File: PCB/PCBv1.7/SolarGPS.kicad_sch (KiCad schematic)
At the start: 38 parts, among them J1 Conn_01x10_Female, J2 GND, J3 GND, J4 Solar1+, J5 Solar2+, J6 Conn_02x03_Odd_Even, J7 Screw_Terminal_01x01, J8 Conn_01x04_Male, SW1 SW_Push, U1 TPS63802, U2 SAM-M10Q, U3 STM32L071KBTx, U4 MAX40200AUK, Y1 32.768

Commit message: Submit board 1.7
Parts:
- removed D1, D2: Schottky, Diode_SMD:D_SOD-323_HandSoldering, symbol Device:D_Schottky_Small
- removed U4: MAX40200AUK, Package_TO_SOT_SMD:SOT-23-5, symbol Analog_Switch:MAX40200AUK
- added D1: 4V, Diode_SMD:D_SMB_Handsoldering, symbol Device:D_Zener
- added U4, U5, U6: LM66100, Package_TO_SOT_SMD:SOT-363_SC-70-6, symbol Heliograph:LM66100
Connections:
- net GND: now also D1.2 (A), U4.2 (GND), U4.5 (ST), U5.2 (GND), U5.5 (ST), U6.2 (GND), U6.5 (ST)
- net GPS_EN: now also U4.3 (EN)
- net GPS_VDD: now also U4.6 (OUT)
- net SOLAR1+: now also U5.1 (VDD)
- net SOLAR2+: now also U6.1 (VDD)
- net VBAT: now also D1.1 (K), U5.3 (EN), U5.6 (OUT), U6.3 (EN), U6.6 (OUT)
- net VDD: now also U4.1 (VDD)
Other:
- moved on the sheet: C1, C10, C4, C5, C6, C7, C8, C9, J3, J5, L1, R2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

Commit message: Tweak PCB
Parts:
- removed D1: 4V, Diode_SMD:D_SMB_Handsoldering, symbol Device:D_Zener
- removed R4: 432k, Resistor_SMD:R_0603_1608Metric, symbol Device:R_Small
- removed SW1: SW_Push, Button_Switch_SMD:SW_SPST_CK_RS282G05A3, symbol Switch:SW_Push
- removed U4, U5, U6: LM66100, Package_TO_SOT_SMD:SOT-363_SC-70-6, symbol Heliograph:LM66100
- added C11: 1uF, Capacitor_SMD:C_0603_1608Metric, symbol Device:C_Small
- added D3: LED_Small, Diode_SMD:D_0805_2012Metric, symbol Device:LED_Small
- added R5: 60, Resistor_SMD:R_0603_1608Metric, symbol Device:R_Small
- added U4: BMI160, digikey-footprints:BMI160, symbol dk_Motion-Sensors-IMUs-Inertial-Measurement-Units:BMI160
- added U5, U6, U7: MAX40200AUK, Package_TO_SOT_SMD:SOT-23-5, symbol Analog_Switch:MAX40200AUK
- C7: value 0.1uF -> 1uF
- R1: value 100 -> 86k
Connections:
- net DISPCS: now also U3.20 (PA10); no longer U3.19 (PA9)
- net GND: now also C11.2, U4.6 (GND), U4.7 (GND), U5.2 (GND), U6.2 (GND), U7.2 (GND)
- net GPS_EN: now also U5.3 (EN)
- net GPS_VDD: now also U5.5 (OUT)
- net LCDEN: now also U3.19 (PA9); no longer U3.18 (PA8)
- net SOLAR1+: now also U6.1 (VDD)
- net SOLAR2+: now also U7.1 (VDD)
- net SPI_CLK: now also U4.13 (SC)
- net SPI_MISO: now also U4.1 (SDO)
- net SPI_MOSI: now also U4.14 (SD)
- net VBAT: now also U6.5 (OUT), U7.5 (OUT)
- net VDD: now also C11.1, R5.1, U4.5 (VDDIO), U4.8 (VDD), U5.1 (VDD)
- net MMU_INT: now reaches U3.14 (PB0)
- net MMU_INT: now also U4.4 (INT1)
- net MMU_CS: now reaches U3.15 (PB1)
- net MMU_CS: now also U4.12 (CSB)
- net LED: now reaches U3.22 (PA12)
- net LED: now also D3.1 (K)
- net Button: no longer names the net of U3.6 (PA0)
- new net: D3.2 (A), R5.2
- new net SOLAREN: U3.18 (PA8), U6.3 (EN), U7.3 (EN)
- no-connect marks 9 -> 20
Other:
- note added: "VEN = 1.1V"
- moved on the sheet: C1, C5, J2, J3, J4, J5, U2

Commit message: add USB!
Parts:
- removed C11, C19: 1uF, Capacitor_SMD:C_0603_1608Metric, symbol Device:C_Small
- removed C5: 4.7uF, Capacitor_SMD:C_0805_2012Metric, symbol Device:C_Small
- removed U3: STM32L071KBTx, Package_QFP:LQFP-32_7x7mm_P0.8mm, symbol MCU_ST_STM32L0:STM32L071KBTx
- added C12, C17: 1uF, Capacitor_SMD:C_0603_1608Metric, symbol Device:C_Small
- added D1: LED_Small, Diode_SMD:D_0805_2012Metric, symbol Device:LED_Small
- added J9: USB_C_Receptacle_USB2.0, Veridian:USB_TYPE_C_PCB, symbol Connector:USB_C_Receptacle_USB2.0
- added R10: 10, Resistor_SMD:R_0805_2012Metric, symbol Device:R_Small
- added R11, R8, R9: 5.1K, Resistor_SMD:R_0603_1608Metric, symbol Device:R_Small
- added R4, R?: 86k, Resistor_SMD:R_0603_1608Metric, symbol Device:R_Small
- added U3: STM32L432KCUx, Package_DFN_QFN:QFN-32-1EP_5x5mm_P0.5mm_EP3.45x3.45mm, symbol MCU_ST_STM32L4:STM32L432KCUx
- added U8: USBLC6-2SC6, Package_TO_SOT_SMD:SOT-23-6, symbol Power_Protection:USBLC6-2SC6
- C10, C9: value 47uF -> 22uF
- C8: value 10nF -> 1uF
- L1: footprint Inductor_SMD:L_0805_2012Metric_Pad1.05x1.20mm_HandSolder -> Inductor_SMD:L_0805_2012Metric_Pad1.15x1.40mm_HandSolder
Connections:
- net DISPCS: now also U3.19 (PA9)
- net GND: now also C12.1, C17.2, J9.A1 (GND), J9.A12 (GND), J9.B1 (GND), J9.B12 (GND), J9.S1 (SHIELD), R8.2, R9.2, U3.16 (VSS), U3.32 (VSS), U3.33 (VSS), U8.2 (GND)
- net GPS_EN: now also U3.10 (PA4)
- net GPS_UART_MISO: now also U3.9 (PA3)
- net GPS_UART_MOSI: now also U3.8 (PA2)
- net LCDEN: now also U3.20 (PA10)
- net LED: now also U3.25 (PA15)
- net MMU_CS: now also U3.15 (PB1)
- net MMU_INT: now also U3.14 (PB0)
- net SOLAR1+: now also R?.2
- net SOLAR2+: now also R4.2
- net SOLAREN: now also R4.1, R?.1, U3.18 (PA8)
- net SPI_CLK: now also U3.11 (PA5)
- net SPI_MISO: now also U3.12 (PA6)
- net SPI_MOSI: now also U3.13 (PA7)
- net SWCLK: now also U3.24 (PA14)
- net SWDIO: now also U3.23 (PA13)
- net VBAT: now also D1.1 (K)
- net VBATSENSE: now also U3.7 (PA1)
- net VDD: now also C12.2, C17.1, U3.1 (VDD), U3.17 (VDD), U3.5 (VDDA)
- net XTAL1: now also U3.2 (PC14)
- net XTAL2: now also U3.3 (PC15)
- net nRESET: now also U3.4 (NRST)
- net at R1.1: now also U3.31 (PH3)
- net UART1TX: no longer names the net of J6.6 (Pin_6)
- new net: D1.2 (A), R10.2
- new net: J9.B5 (CC2), R9.1
- new net: R11.2, U3.28 (PB5)
- new net: J9.A5 (CC1), R8.1
- new net USBR_N: J9.A7 (D-), J9.B7 (D-), U8.1 (I/O1)
- new net USBR_P: J9.A6 (D+), J9.B6 (D+), U8.3 (I/O2)
- new net USB_N: U3.21 (PA11), U8.6 (I/O1)
- new net USB_P: U3.22 (PA12), U8.4 (I/O2)
- new net VUSB: J9.A4 (VBUS), J9.A9 (VBUS), J9.B4 (VBUS), J9.B9 (VBUS), R10.1, R11.1, U8.5 (VBUS)
- no-connect marks 20 -> 21
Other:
- note added: "Hybrid Super Cap Rated 2.2-3.8VDC"
- note added: "MOTION"
- note added: "USB"
- moved on the sheet: C1, C13, C14, C15, C16, C2, D3, J8, L1, R1, R5, U4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

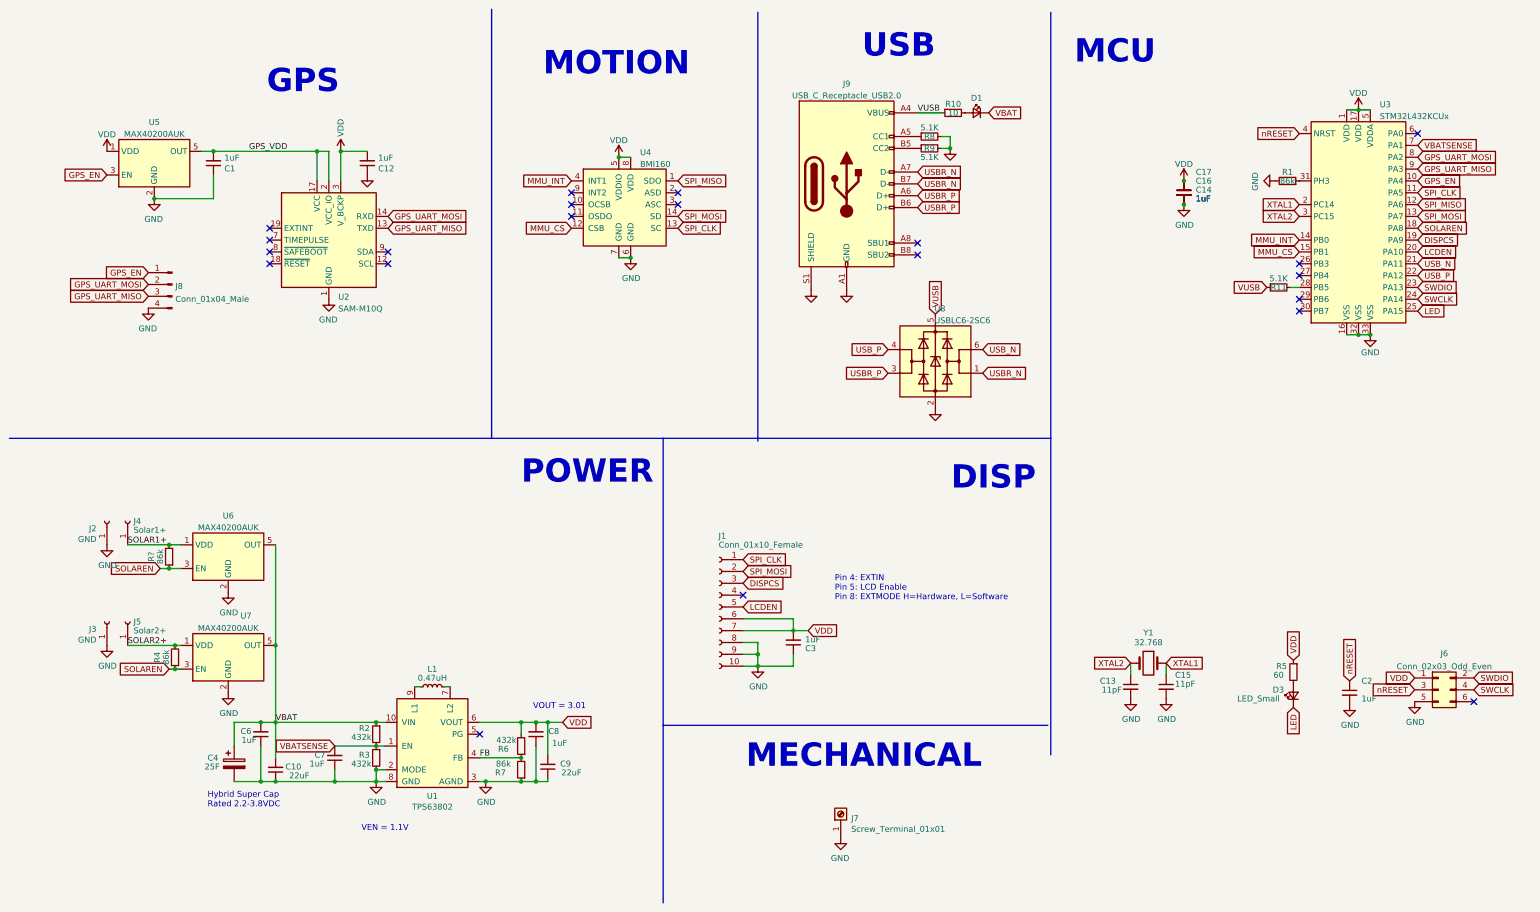
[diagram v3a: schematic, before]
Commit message: Add USB pulldown and SWO
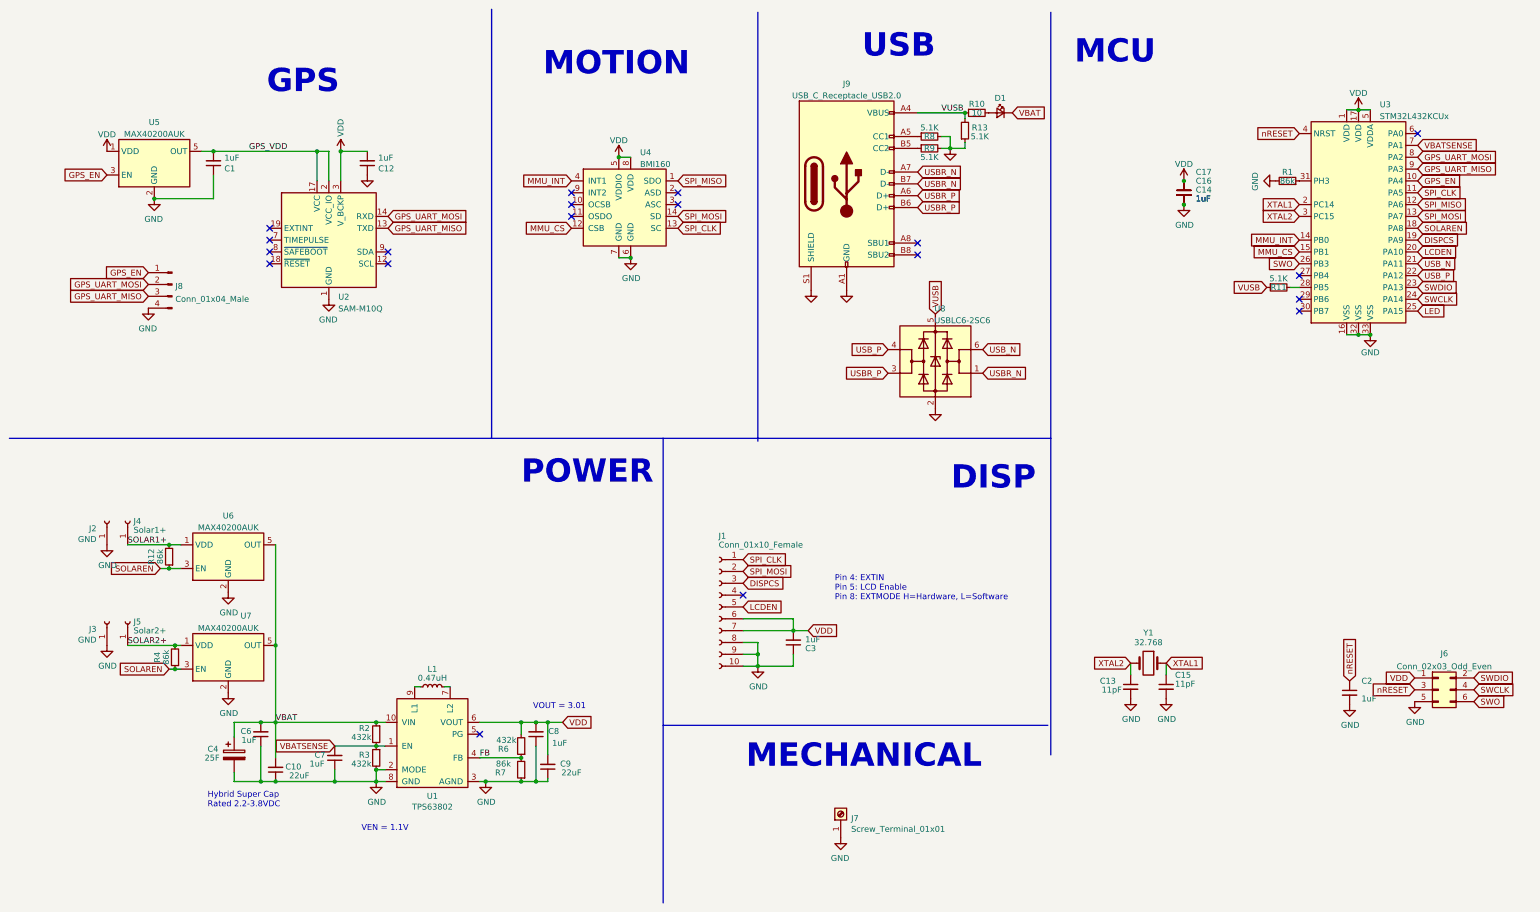
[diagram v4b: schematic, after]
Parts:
- removed D3: LED_Small, Diode_SMD:D_0805_2012Metric, symbol Device:LED_Small
- removed R5: 60, Resistor_SMD:R_0603_1608Metric, symbol Device:R_Small
- added R13: 5.1K, Resistor_SMD:R_0603_1608Metric, symbol Device:R_Small
- gave numbers to parts that had none: 1
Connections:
- net GND: now also R13.1
- net VUSB: now also R13.2
- net SWO: now reaches J6.6 (Pin_6)
- net SWO: now also U3.26 (PB3)
- no-connect marks 21 -> 19
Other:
- moved on the sheet: C4, D1, R10

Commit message: Do PCB 1.7
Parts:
- C4: value 25F -> 70F
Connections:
- net nRESET: no longer U3.4 (NRST)
- net EXTIN: now reaches J1.4 (Pin_4)
- no-connect marks 19 -> 18
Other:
- moved on the sheet: C10, C4, C6, C7, C8, C9, J1, J2, J3, J4, J5, L1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

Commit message: Tweak Resistors
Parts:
- R1, R12, R4, R7: value 86k -> 86.6k
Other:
- note added: "VOUT = 3.0"
- note removed: "VOUT = 3.01"
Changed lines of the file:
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@@
     (effects (font (size 5.0038 5.0038) (thickness 1.0008) bold) (justify left bottom))
   )
-  (text "VOUT = 3.01" (at 125.095 167.513 0)
+  (text "VOUT = 3.0" (at 125.095 167.513 0)
     (effects (font (size 1.27 1.27)) (justify left bottom))
   )
@@
     (in_bom yes) (on_board yes)
     (property "Reference" "R12" (id 0) (at 43.18 134.62 90))
-    (property "Value" "86k" (id 1) (at 45.085 134.62 90))
+    (property "Value" "86.6k" (id 1) (at 45.085 134.62 90))
     (property "Footprint" "Resistor_SMD:R_0603_1608Metric" (id 2) (at 46.99 134.62 0)
       (effects (font (size 1.27 1.27)) hide)
@@
     (in_bom yes) (on_board yes)
     (property "Reference" "R4" (id 0) (at 44.45 156.21 90))
-    (property "Value" "86k" (id 1) (at 46.355 156.21 90))
+    (property "Value" "86.6k" (id 1) (at 46.355 156.21 90))
     (property "Footprint" "Resistor_SMD:R_0603_1608Metric" (id 2) (at 48.26 156.21 0)
       (effects (font (size 1.27 1.27)) hide)
@@
     (in_bom yes) (on_board yes)
     (property "Reference" "R7" (id 0) (at 118.11 180.975 0))
-    (property "Value" "86k" (id 1) (at 118.745 179.07 0))
+    (property "Value" "86.6k" (id 1) (at 118.745 179.07 0))
     (property "Footprint" "Resistor_SMD:R_0603_1608Metric" (id 2) (at 122.555 180.34 0)
       (effects (font (size 1.27 1.27)) hide)
@@
     (in_bom yes) (on_board yes)
     (property "Reference" "R1" (id 0) (at 287.02 46.355 90))
-    (property "Value" "86k" (id 1) (at 287.02 48.26 90))
+    (property "Value" "86.6k" (id 1) (at 287.02 48.26 90))
     (property "Footprint" "Resistor_SMD:R_0603_1608Metric" (id 2) (at 287.02 48.26 0)
       (effects (font (size 1.27 1.27)) hide)
@@
     )
     (path "/c1d4681b-f4ba-405d-9632-bf584a81375a"
-      (reference "R1") (unit 1) (value "86k") (footprint "Resistor_SMD:R_0603_1608Metric")
+      (reference "R1") (unit 1) (value "86.6k") (footprint "Resistor_SMD:R_0603_1608Metric")
     )
     (path "/08f15c76-b017-4c6c-91c0-1c3f0ff60f39"
@@
     )
     (path "/66ab1b6c-c0f7-4e17-aa5a-633f1b282017"
-      (reference "R4") (unit 1) (value "86k") (footprint "Resistor_SMD:R_0603_1608Metric")
+      (reference "R4") (unit 1) (value "86.6k") (footprint "Resistor_SMD:R_0603_1608Metric")
     )
     (path "/b7fb5cdf-ae9c-4fee-86cd-85cb4152df62"
@@
     )
     (path "/8c70be32-1219-4d69-a829-74b183f2f44f"
-      (reference "R7") (unit 1) (value "86k") (footprint "Resistor_SMD:R_0603_1608Metric")
+      (reference "R7") (unit 1) (value "86.6k") (footprint "Resistor_SMD:R_0603_1608Metric")
     )
     (path "/bd46e7cc-b93d-421d-a647-5afb3f41c47c"
@@
     )
     (path "/3ca7f24b-5230-4198-9368-e2eee124f640"
-      (reference "R12") (unit 1) (value "86k") (footprint "Resistor_SMD:R_0603_1608Metric")
+      (reference "R12") (unit 1) (value "86.6k") (footprint "Resistor_SMD:R_0603_1608Metric")
     )
     (path "/53efff7a-a39b-49e0-a104-fa1d9eddbd94"
